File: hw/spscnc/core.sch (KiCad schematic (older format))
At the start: 41 parts, among them J11 Conn_01x04, J7 USB_B_Micro, Q11 BSP41, Q12 BSP42, U3 NCP1117ST33T3G, U4 ESP32-WROOM-32D, U8 FT232RL

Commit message: .
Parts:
- added R? (x4): 47, Resistor_SMD:R_0805_2012Metric, symbol Device:R_Small
- added R? (x2): 1K, Resistor_SMD:R_0603_1608Metric, symbol Device:R_Small
- added U?: 74HC595, symbol 74xx:74HCT595
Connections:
- net labels added: DIR_A, DIR_B, I2S_BITCLK, I2S_DATA, I2S_WORDSTROBE, MTDI, STEP_A, STEP_B, ~I2S_ENABLE
- wire segments 91 -> 101
- no-connect marks 16 -> 17
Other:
- note added: "BOOT MODE:\nMTDI 0 => 3v3 SPI\nGPIO0 1 => Boot APP\nGPIO2 0 => Download\nMTDO 0 => Silent UART / SDIO Sample Fall\nGPIO5 SDIO Launch Fall"
- note added: "TODO:\nchange fluidnc config and attempt to boot.\ncheck bootmode is ok with GPIO signals\ncheck pulses during boot on output pins.\n"
- moved on the sheet: C27, C29, D10, R172, R179, R180, R181, R54, U4

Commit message: halfway changes to support additional axis and to extend over i2so
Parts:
- removed R172, R?: 1K, Resistor_SMD:R_0603_1608Metric, symbol Device:R_Small
- removed R? (x4): 47, Resistor_SMD:R_0805_2012Metric, symbol Device:R_Small
- removed U?: 74HC595, symbol 74xx:74HCT595
- added R187, R188, R189, R190: 47, Resistor_SMD:R_0805_2012Metric, symbol Device:R_Small
- added R191, R64, R65: 1K, Resistor_SMD:R_0603_1608Metric, symbol Device:R_Small
- added U13, U14: 74HC595, symbol 74xx:74HCT595
- gave numbers to parts that had none: 1
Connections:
- net labels added: I2SB
- wire segments 101 -> 113
- no-connect marks 17 -> 23
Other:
- moved on the sheet: C27, C29, C31, C32, C33, D10, R172, R175, R176, R177, R178, R182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

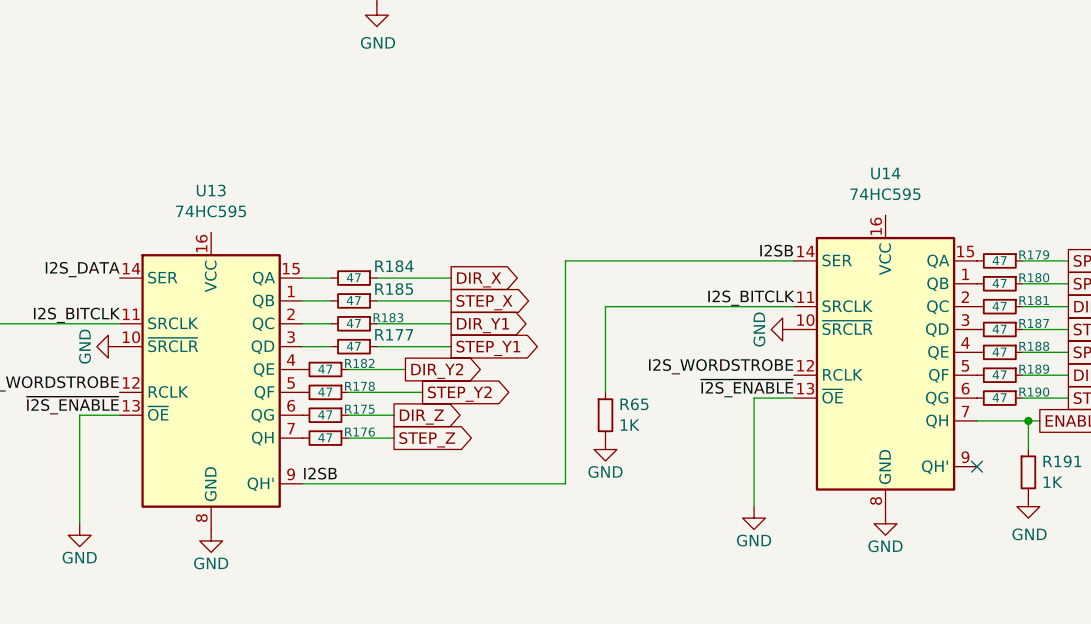
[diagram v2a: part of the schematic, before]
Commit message: added most corrections on the schematic for i2s operation.
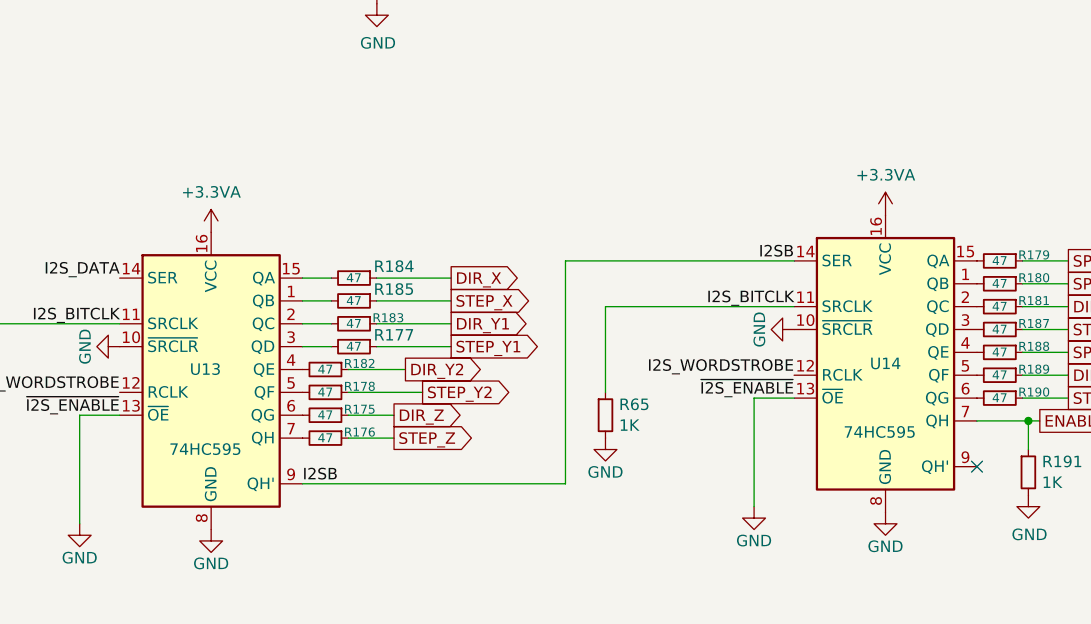
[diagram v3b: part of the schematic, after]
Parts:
- U13, U14: footprint (none) -> Package_SO:SOIC-16_3.9x9.9mm_P1.27mm
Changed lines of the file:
@@
 $Descr A4 11693 8268
 encoding utf-8
-Sheet 6 16
+Sheet 6 17
 Title "Trinamic FluidNC CNC Controller"
 Date "2022-01-27"
@@
 U 1 1 62063E4D
 P 6000 5275
-F 0 "U13" H 6000 6056 50  0000 C CNN
-F 1 "74HC595" H 6000 5965 50  0000 C CNN
-F 2 "" H 6000 5275 50  0001 C CNN
+F 0 "U13" H 5975 5275 50  0000 C CNN
+F 1 "74HC595" H 5975 4925 50  0000 C CNN
+F 2 "Package_SO:SOIC-16_3.9x9.9mm_P1.27mm" H 6000 5275 50  0001 C CNN
 F 3 "https://assets.nexperia.com/documents/data-sheet/74HC_HCT595.pdf" H 6000 5275 50  0001 C CNN
 F 4 "C5947" H 6000 5275 50  0001 C CNN "jlcpcb"
@@
 U 1 1 620F06E6
 P 8950 5200
-F 0 "U14" H 8950 5981 50  0000 C CNN
-F 1 "74HC595" H 8950 5890 50  0000 C CNN
-F 2 "" H 8950 5200 50  0001 C CNN
+F 0 "U14" H 8950 5150 50  0000 C CNN
+F 1 "74HC595" H 8925 4850 50  0000 C CNN
+F 2 "Package_SO:SOIC-16_3.9x9.9mm_P1.27mm" H 8950 5200 50  0001 C CNN
 F 3 "https://assets.nexperia.com/documents/data-sheet/74HC_HCT595.pdf" H 8950 5200 50  0001 C CNN
 F 4 "C5947" H 8950 5200 50  0001 C CNN "jlcpcb"
@@
 NoConn ~ 7375 2775
 NoConn ~ 7325 1475
+$Comp
+L power:+3.3VA-power #PWR?
+U 1 1 623077B6
+P 6000 4675
+AR Path="/61367F02/623077B6" Ref="#PWR?"  Part="1"
+AR Path="/5AD46BE5/619A452E/61B9A8A6/623077B6" Ref="#PWR?"  Part="1"
+AR Path="/61B9A8A6/623077B6" Ref="#PWR?"  Part="1"
+AR Path="/61C743E7/61B9A8A6/623077B6" Ref="#PWR?"  Part="1"
+AR Path="/61C81F9D/623077B6" Ref="#PWR0266"  Part="1"
+AR Path="/623077B6" Ref="#PWR?"  Part="1"
+F 0 "#PWR0266" H 6000 4525 50  0001 C CNN
+F 1 "+3.3VA" H 6000 4850 50  0000 C CNN
+F 2 "" H 6000 4675 50  0001 C CNN
+F 3 "" H 6000 4675 50  0001 C CNN
+	1    6000 4675
+	1    0    0    -1
+$EndComp
+$Comp
+L power:+3.3VA-power #PWR?
+U 1 1 6230AD42
+P 8950 4600
+AR Path="/61367F02/6230AD42" Ref="#PWR?"  Part="1"
+AR Path="/5AD46BE5/619A452E/61B9A8A6/6230AD42" Ref="#PWR?"  Part="1"
+AR Path="/61B9A8A6/6230AD42" Ref="#PWR?"  Part="1"
+AR Path="/61C743E7/61B9A8A6/6230AD42" Ref="#PWR?"  Part="1"
+AR Path="/61C81F9D/6230AD42" Ref="#PWR0267"  Part="1"
+AR Path="/6230AD42" Ref="#PWR?"  Part="1"
+F 0 "#PWR0267" H 8950 4450 50  0001 C CNN
+F 1 "+3.3VA" H 8950 4775 50  0000 C CNN
+F 2 "" H 8950 4600 50  0001 C CNN
+F 3 "" H 8950 4600 50  0001 C CNN
+	1    8950 4600
+	1    0    0    -1
+$EndComp
 $EndSCHEMATC

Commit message: Improved and validated config file
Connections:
- wire segments 113 -> 114
- no-connect marks 23 -> 21
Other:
- moved on the sheet: R180, R188, R191
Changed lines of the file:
@@
 Wire Wire Line
 	7375 2775 7325 2775
-Wire Wire Line
-	7375 2875 7325 2875
 Text GLabel 7325 3275 2    50   Input ~ 0
 LIM_Y1
@@
 Text Notes 12525 3900 0    50   ~ 0
 TODO:\nchange fluidnc config and attempt to boot.\ncheck bootmode is ok with GPIO signals\ncheck pulses during boot on output pins.\n
-Text GLabel 9750 4900 2    50   Output ~ 0
+Text GLabel 7775 1475 2    50   Output ~ 0
 SPINDLE_EN
-Text GLabel 9625 5500 2    50   Output ~ 0
+Text GLabel 8650 2875 2    50   Output ~ 0
 ENABLE_STEPPERS
-Text GLabel 9750 5200 2    50   Output ~ 0
+Text GLabel 7800 2075 2    50   Output ~ 0
 SPINDLE_PWM
 Text GLabel 9750 4800 2    50   Output ~ 0
@@
 L Device:R_Small R?
 U 1 1 62063E2A
-P 9575 5725
+P 8600 3100
 AR Path="/61367F02/62063E2A" Ref="R?"  Part="1"
 AR Path="/5AD46BE5/619A452E/61B9A8A6/62063E2A" Ref="R?"  Part="1"
@@
 AR Path="/61C743E7/61B9A8A6/62063E2A" Ref="R?"  Part="1"
 AR Path="/61C81F9D/62063E2A" Ref="R191"  Part="1"
-F 0 "R191" H 9634 5771 50  0000 L CNN
-F 1 "1K" H 9634 5680 50  0000 L CNN
-F 2 "Resistor_SMD:R_0603_1608Metric" H 9575 5725 50  0001 C CNN
-F 3 "~" H 9575 5725 50  0001 C CNN
-F 4 "C21190" H 9575 5725 50  0001 C CNN "jlcpcb"
-	1    9575 5725
+F 0 "R191" H 8659 3146 50  0000 L CNN
+F 1 "1K" H 8659 3055 50  0000 L CNN
+F 2 "Resistor_SMD:R_0603_1608Metric" H 8600 3100 50  0001 C CNN
+F 3 "~" H 8600 3100 50  0001 C CNN
+F 4 "C21190" H 8600 3100 50  0001 C CNN "jlcpcb"
+	1    8600 3100
 	1    0    0    -1
 $EndComp
@@
 L power:GND-power #PWR?
 U 1 1 62063E31
-P 9575 5825
+P 8600 3200
 AR Path="/61367F02/62063E31" Ref="#PWR?"  Part="1"
 AR Path="/5AD46BE5/619A452E/61B9A8A6/62063E31" Ref="#PWR?"  Part="1"
@@
 AR Path="/61C81F9D/62063E31" Ref="#PWR0129"  Part="1"
 AR Path="/62063E31" Ref="#PWR?"  Part="1"
-F 0 "#PWR0129" H 9575 5575 50  0001 C CNN
-F 1 "GND" H 9580 5652 50  0000 C CNN
-F 2 "" H 9575 5825 50  0001 C CNN
-F 3 "" H 9575 5825 50  0001 C CNN
-	1    9575 5825
+F 0 "#PWR0129" H 8600 2950 50  0001 C CNN
+F 1 "GND" H 8605 3027 50  0000 C CNN
+F 2 "" H 8600 3200 50  0001 C CNN
+F 3 "" H 8600 3200 50  0001 C CNN
+	1    8600 3200
 	1    0    0    -1
 $EndComp
@@
 L Device:R_Small R?
 U 1 1 62063E3F
-P 9450 5200
+P 7500 2075
 AR Path="/62063E3F" Ref="R?"  Part="1"
 AR Path="/61C81F9D/62063E3F" Ref="R188"  Part="1"
-F 0 "R188" V 9425 5350 39  0000 C CNN
-F 1 "47" V 9450 5200 39  0000 C CNN
-F 2 "Resistor_SMD:R_0805_2012Metric" V 9380 5200 50  0001 C CNN
-F 3 "~" H 9450 5200 50  0001 C CNN
-F 4 "C17714" H 9450 5200 50  0001 C CNN "jlcpcb"
-	1    9450 5200
+F 0 "R188" V 7475 2225 39  0000 C CNN
+F 1 "47" V 7500 2075 39  0000 C CNN
+F 2 "Resistor_SMD:R_0805_2012Metric" V 7430 2075 50  0001 C CNN
+F 3 "~" H 7500 2075 50  0001 C CNN
+F 4 "C17714" H 7500 2075 50  0001 C CNN "jlcpcb"
+	1    7500 2075
 	0    1    1    0
 $EndComp
@@
 L Device:R_Small R?
 U 1 1 62063E46
-P 9450 4900
+P 7475 1475
 AR Path="/62063E46" Ref="R?"  Part="1"
 AR Path="/61C81F9D/62063E46" Ref="R180"  Part="1"
-F 0 "R180" V 9425 5050 39  0000 C CNN
-F 1 "47" V 9450 4900 39  0000 C CNN
-F 2 "Resistor_SMD:R_0805_2012Metric" V 9380 4900 50  0001 C CNN
-F 3 "~" H 9450 4900 50  0001 C CNN
-F 4 "C17714" H 9450 4900 50  0001 C CNN "jlcpcb"
-	1    9450 4900
+F 0 "R180" V 7450 1625 39  0000 C CNN
+F 1 "47" V 7475 1475 39  0000 C CNN
+F 2 "Resistor_SMD:R_0805_2012Metric" V 7405 1475 50  0001 C CNN
+F 3 "~" H 7475 1475 50  0001 C CNN
+F 4 "C17714" H 7475 1475 50  0001 C CNN "jlcpcb"
+	1    7475 1475
 	0    1    1    0
 $EndComp
@@
 	9750 4800 9550 4800
 Wire Wire Line
-	9550 5200 9750 5200
-Wire Wire Line
-	9550 4900 9750 4900
+	7600 2075 7800 2075
+Wire Wire Line
+	7575 1475 7775 1475
 Text GLabel 9750 5000 2    50   Output ~ 0
 DIR_A
@@
 	8375 5400 8375 5875
 Wire Wire Line
-	9575 5625 9575 5500
-Connection ~ 9575 5500
-Wire Wire Line
-	9575 5500 9625 5500
-Wire Wire Line
-	9350 5500 9575 5500
+	8600 3000 8600 2875
+Connection ~ 8600 2875
+Wire Wire Line
+	8600 2875 8650 2875
 Text Label 6400 5775 0    50   ~ 0
 I2SB
@@
 NoConn ~ 7325 1775
 NoConn ~ 7325 1875
-NoConn ~ 7325 2075
-NoConn ~ 7375 2875
 NoConn ~ 7375 2775
-NoConn ~ 7325 1475
 $Comp
 L power:+3.3VA-power #PWR?
@@
 	1    0    0    -1
 $EndComp
+Wire Wire Line
+	7325 2875 8600 2875
+NoConn ~ 9350 5500
+Wire Wire Line
+	7375 1475 7325 1475
+Wire Wire Line
+	7400 2075 7325 2075
 $EndSCHEMATC

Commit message: began routing of the i2so part
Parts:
- removed R65: 1K, Resistor_SMD:R_0603_1608Metric, symbol Device:R_Small
- added C91, C92: 100nF, Capacitor_SMD:C_0603_1608Metric, symbol Device:C
- added D55: LED, Diode_SMD:D_0805_2012Metric, symbol Device:LED
- added R194: 10K, Resistor_SMD:R_0805_2012Metric, symbol Device:R
- added R195, R196: 47, Resistor_SMD:R_0805_2012Metric, symbol Device:R_Small
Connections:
- net labels added: ENABLE_VACUUM
- wire segments 114 -> 118
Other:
- note added: "CHECKS:\n[OK] change fluidnc config and attempt to boot.\n[OK] check bootmode is ok with GPIO signals\ncheck pulses during boot on output pins.\n"
- note removed: "TODO:\nchange fluidnc config and attempt to boot.\ncheck bootmode is ok with GPIO signals\ncheck pulses during boot on output pins.\n"
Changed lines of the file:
@@
 Text GLabel 6125 1375 0    50   Input ~ 0
 Hold
-Text GLabel 8625 1675 2    50   Input ~ 0
+Text GLabel 8800 1675 2    50   Input ~ 0
 Reset
 Text GLabel 7475 3175 2    50   Input ~ 0
 Door
 Wire Wire Line
-	8625 1675 8500 1675
+	8800 1675 8500 1675
 Wire Wire Line
 	7325 1975 7425 1975
@@
 Wire Wire Line
 	6800 5575 6600 5575
-Text Label 7450 2575 0    50   ~ 0
+Text Label 8125 2575 0    50   ~ 0
 I2S_BITCLK
-Text Label 7450 2475 0    50   ~ 0
+Text Label 8125 2475 0    50   ~ 0
 I2S_DATA
 Text Label 7450 2175 0    50   ~ 0
@@
 BOOT MODE:\nMTDI 0 => 3v3 SPI\nGPIO0 1 => Boot APP\nGPIO2 0 => Download\nMTDO 0 => Silent UART / SDIO Sample Fall\nGPIO5 SDIO Launch Fall
 Text Notes 12525 3900 0    50   ~ 0
-TODO:\nchange fluidnc config and attempt to boot.\ncheck bootmode is ok with GPIO signals\ncheck pulses during boot on output pins.\n
+CHECKS:\n[OK] change fluidnc config and attempt to boot.\n[OK] check bootmode is ok with GPIO signals\ncheck pulses during boot on output pins.\n
 Text GLabel 7775 1475 2    50   Output ~ 0
 SPINDLE_EN
@@
 Text Label 8550 5400 2    50   ~ 0
 ~I2S_ENABLE
-Wire Wire Line
-	8550 5000 7725 5000
-Wire Wire Line
-	7725 5000 7725 5375
-$Comp
-L Device:R_Small R?
-U 1 1 620F09CF
-P 7725 5475
-AR Path="/61367F02/620F09CF" Ref="R?"  Part="1"
-AR Path="/5AD46BE5/619A452E/61B9A8A6/620F09CF" Ref="R?"  Part="1"
-AR Path="/61B9A8A6/620F09CF" Ref="R?"  Part="1"
-AR Path="/61C743E7/61B9A8A6/620F09CF" Ref="R?"  Part="1"
-AR Path="/61C81F9D/620F09CF" Ref="R65"  Part="1"
-F 0 "R65" H 7784 5521 50  0000 L CNN
-F 1 "1K" H 7784 5430 50  0000 L CNN
-F 2 "Resistor_SMD:R_0603_1608Metric" H 7725 5475 50  0001 C CNN
-F 3 "~" H 7725 5475 50  0001 C CNN
-F 4 "C21190" H 7725 5475 50  0001 C CNN "jlcpcb"
-	1    7725 5475
-	1    0    0    -1
-$EndComp
-$Comp
-L power:GND-power #PWR?
-U 1 1 620F09D9
-P 7725 5575
-AR Path="/5AD46BE5/620F09D9" Ref="#PWR?"  Part="1"
-AR Path="/5AD46BE5/619A452E/620F09D9" Ref="#PWR?"  Part="1"
-AR Path="/620F09D9" Ref="#PWR?"  Part="1"
-AR Path="/61B9A8A6/620F09D9" Ref="#PWR?"  Part="1"
-AR Path="/61C743E7/61B9A8A6/620F09D9" Ref="#PWR?"  Part="1"
-AR Path="/61C81F9D/620F09D9" Ref="#PWR063"  Part="1"
-F 0 "#PWR063" H 7725 5325 50  0001 C CNN
-F 1 "GND" H 7725 5425 50  0000 C CNN
-F 2 "" H 7725 5575 50  0001 C CNN
-F 3 "" H 7725 5575 50  0001 C CNN
-	1    7725 5575
-	-1   0    0    -1
-$EndComp
 $Comp
 L power:GND-power #PWR?
@@
 Wire Wire Line
 	7325 2875 8600 2875
-NoConn ~ 9350 5500
 Wire Wire Line
 	7375 1475 7325 1475
 Wire Wire Line
 	7400 2075 7325 2075
+NoConn ~ 9350 5200
+$Comp
+L Device:R R?
+U 1 1 620708E2
+P 9675 6100
+AR Path="/5AD47FD6/620708E2" Ref="R?"  Part="1"
+AR Path="/61FBB705/620708E2" Ref="R?"  Part="1"
+AR Path="/5AD46BE5/620708E2" Ref="R?"  Part="1"
+AR Path="/5AD46BE5/619A452E/620708E2" Ref="R?"  Part="1"
+AR Path="/620708E2" Ref="R?"  Part="1"
+AR Path="/61B9A8A6/620708E2" Ref="R?"  Part="1"
+AR Path="/61C743E7/61B9A8A6/620708E2" Ref="R?"  Part="1"
+AR Path="/61C81F9D/620708E2" Ref="R194"  Part="1"
+F 0 "R194" V 9755 6100 50  0000 C CNN
+F 1 "10K" V 9675 6100 50  0000 C CNN
+F 2 "Resistor_SMD:R_0805_2012Metric" V 9605 6100 50  0001 C CNN
+F 3 "" H 9675 6100 50  0001 C CNN
+F 4 "" V 9675 6100 60  0001 C CNN "farnell"
+F 5 "C17414" H 9675 6100 50  0001 C CNN "jlcpcb"
+F 6 "5%" H 9675 6100 50  0001 C CNN "precision"
+F 7 "1%" H 9675 6100 50  0001 C CNN "power"
+	1    9675 6100
+	1    0    0    -1
+$EndComp
+$Comp
+L Device:LED D?
+U 1 1 620708EF
+P 9675 5750
+AR Path="/5AD47FD6/620708EF" Ref="D?"  Part="1"
+AR Path="/61FBB705/620708EF" Ref="D?"  Part="1"
+AR Path="/5AD46BE5/620708EF" Ref="D?"  Part="1"
+AR Path="/5AD46BE5/619A452E/620708EF" Ref="D?"  Part="1"
+AR Path="/620708EF" Ref="D?"  Part="1"
+AR Path="/61B9A8A6/620708EF" Ref="D?"  Part="1"
+AR Path="/61C743E7/61B9A8A6/620708EF" Ref="D?"  Part="1"
+AR Path="/61C81F9D/620708EF" Ref="D55"  Part="1"
+F 0 "D55" H 9675 5850 50  0000 C CNN
+F 1 "LED" H 9675 5650 50  0000 C CNN
+F 2 "Diode_SMD:D_0805_2012Metric" H 9675 5750 50  0001 C CNN
+F 3 "" H 9675 5750 50  0001 C CNN
+F 4 "" H 9675 5750 60  0001 C CNN "farnell"
+F 5 "C84256" H 9675 5750 50  0001 C CNN "jlcpcb"
+F 6 "red" H 9675 5750 50  0001 C CNN "power"
+	1    9675 5750
+	0    -1   -1   0
+$EndComp
+Wire Wire Line
+	9675 5950 9675 5900
+Wire Wire Line
+	9350 5500 9675 5500
+Wire Wire Line
+	9675 5500 9675 5600
+$Comp
+L power:GND-power #PWR?
+U 1 1 62082702
+P 9675 6250
+AR Path="/5AD46BE5/62082702" Ref="#PWR?"  Part="1"
+AR Path="/5AD46BE5/619A452E/62082702" Ref="#PWR?"  Part="1"
+AR Path="/62082702" Ref="#PWR?"  Part="1"
+AR Path="/61B9A8A6/62082702" Ref="#PWR?"  Part="1"
+AR Path="/61C743E7/61B9A8A6/62082702" Ref="#PWR?"  Part="1"
+AR Path="/61C81F9D/62082702" Ref="#PWR0268"  Part="1"
+F 0 "#PWR0268" H 9675 6000 50  0001 C CNN
+F 1 "GND" H 9675 6100 50  0000 C CNN
+F 2 "" H 9675 6250 50  0001 C CNN
+F 3 "" H 9675 6250 50  0001 C CNN
+	1    9675 6250
+	-1   0    0    -1
+$EndComp
+$Comp
+L Device:R_Small R?
+U 1 1 62091D8C
+P 7550 2475
+AR Path="/62091D8C" Ref="R?"  Part="1"
+AR Path="/61C81F9D/62091D8C" Ref="R195"  Part="1"
+F 0 "R195" V 7500 2650 50  0000 C CNN
+F 1 "47" V 7550 2475 39  0000 C CNN
+F 2 "Resistor_SMD:R_0805_2012Metric" V 7480 2475 50  0001 C CNN
+F 3 "~" H 7550 2475 50  0001 C CNN
+F 4 "C17714" H 7550 2475 50  0001 C CNN "jlcpcb"
+	1    7550 2475
+	0    1    1    0
+$EndComp
+$Comp
+L Device:R_Small R?
+U 1 1 620A09FA
+P 7550 2575
+AR Path="/620A09FA" Ref="R?"  Part="1"
+AR Path="/61C81F9D/620A09FA" Ref="R196"  Part="1"
+F 0 "R196" V 7500 2750 50  0000 C CNN
+F 1 "47" V 7550 2575 39  0000 C CNN
+F 2 "Resistor_SMD:R_0805_2012Metric" V 7480 2575 50  0001 C CNN
+F 3 "~" H 7550 2575 50  0001 C CNN
+F 4 "C17714" H 7550 2575 50  0001 C CNN "jlcpcb"
+	1    7550 2575
+	0    1    1    0
+$EndComp
+Wire Wire Line
+	7650 2575 8125 2575
+Wire Wire Line
+	8125 2475 7650 2475
+Text GLabel 9750 4900 2    50   Output ~ 0
+ENABLE_VACUUM
+Wire Wire Line
+	9750 4900 9350 4900
+$Comp
+L Device:C C?
+U 1 1 621362CC
+P 5825 6975
+AR Path="/61E601B6/621362CC" Ref="C?"  Part="1"
+AR Path="/6203D74D/621362CC" Ref="C?"  Part="1"
+AR Path="/6203DA5D/621362CC" Ref="C?"  Part="1"
+AR Path="/6203DFCF/621362CC" Ref="C?"  Part="1"
+AR Path="/6221509B/621362CC" Ref="C?"  Part="1"
+AR Path="/61C81F9D/621362CC" Ref="C91"  Part="1"
+F 0 "C91" V 6100 7000 50  0000 C CNN
+F 1 "100nF" V 5975 6950 50  0000 C CNN
+F 2 "Capacitor_SMD:C_0603_1608Metric" H 5863 6825 50  0001 C CNN
+F 3 "~" H 5825 6975 50  0001 C CNN
+F 4 "C14663" H 5825 6975 50  0001 C CNN "jlcpcb"
+	1    5825 6975
+	-1   0    0    1
+$EndComp
+$Comp
+L Device:C C?
+U 1 1 6213BF1D
+P 6275 6975
+AR Path="/61E601B6/6213BF1D" Ref="C?"  Part="1"
+AR Path="/6203D74D/6213BF1D" Ref="C?"  Part="1"
+AR Path="/6203DA5D/6213BF1D" Ref="C?"  Part="1"
+AR Path="/6203DFCF/6213BF1D" Ref="C?"  Part="1"
+AR Path="/6221509B/6213BF1D" Ref="C?"  Part="1"
+AR Path="/61C81F9D/6213BF1D" Ref="C92"  Part="1"
+F 0 "C92" V 6550 7000 50  0000 C CNN
+F 1 "100nF" V 6425 6950 50  0000 C CNN
+F 2 "Capacitor_SMD:C_0603_1608Metric" H 6313 6825 50  0001 C CNN
+F 3 "~" H 6275 6975 50  0001 C CNN
+F 4 "C14663" H 6275 6975 50  0001 C CNN "jlcpcb"
+	1    6275 6975
+	-1   0    0    1
+$EndComp
+$Comp
+L power:GND-power #PWR?
+U 1 1 621409CC
+P 6275 7125
+AR Path="/5AD46BE5/621409CC" Ref="#PWR?"  Part="1"
+AR Path="/5AD46BE5/619A452E/621409CC" Ref="#PWR?"  Part="1"
+AR Path="/621409CC" Ref="#PWR?"  Part="1"
+AR Path="/61B9A8A6/621409CC" Ref="#PWR?"  Part="1"
+AR Path="/61C743E7/61B9A8A6/621409CC" Ref="#PWR?"  Part="1"
+AR Path="/61C81F9D/621409CC" Ref="#PWR0168"  Part="1"
+F 0 "#PWR0168" H 6275 6875 50  0001 C CNN
+F 1 "GND" H 6275 6975 50  0000 C CNN
+F 2 "" H 6275 7125 50  0001 C CNN
+F 3 "" H 6275 7125 50  0001 C CNN
+	1    6275 7125
+	-1   0    0    -1
+$EndComp
+$Comp
+L power:GND-power #PWR?
+U 1 1 62140D17
+P 5825 7125
+AR Path="/5AD46BE5/62140D17" Ref="#PWR?"  Part="1"
+AR Path="/5AD46BE5/619A452E/62140D17" Ref="#PWR?"  Part="1"
+AR Path="/62140D17" Ref="#PWR?"  Part="1"
+AR Path="/61B9A8A6/62140D17" Ref="#PWR?"  Part="1"
+AR Path="/61C743E7/61B9A8A6/62140D17" Ref="#PWR?"  Part="1"
+AR Path="/61C81F9D/62140D17" Ref="#PWR0164"  Part="1"
+F 0 "#PWR0164" H 5825 6875 50  0001 C CNN
+F 1 "GND" H 5825 6975 50  0000 C CNN
+F 2 "" H 5825 7125 50  0001 C CNN
+F 3 "" H 5825 7125 50  0001 C CNN
+	1    5825 7125
+	-1   0    0    -1
+$EndComp
+$Comp
+L power:+3.3VA-power #PWR?
+U 1 1 621421A9
+P 5825 6825
+AR Path="/61367F02/621421A9" Ref="#PWR?"  Part="1"
+AR Path="/5AD46BE5/619A452E/61B9A8A6/621421A9" Ref="#PWR?"  Part="1"
+AR Path="/61B9A8A6/621421A9" Ref="#PWR?"  Part="1"
+AR Path="/61C743E7/61B9A8A6/621421A9" Ref="#PWR?"  Part="1"
+AR Path="/61C81F9D/621421A9" Ref="#PWR063"  Part="1"
+AR Path="/621421A9" Ref="#PWR?"  Part="1"
+F 0 "#PWR063" H 5825 6675 50  0001 C CNN
+F 1 "+3.3VA" H 5825 7000 50  0000 C CNN
+F 2 "" H 5825 6825 50  0001 C CNN
+F 3 "" H 5825 6825 50  0001 C CNN
+	1    5825 6825
+	1    0    0    -1
+$EndComp
+$Comp
+L power:+3.3VA-power #PWR?
+U 1 1 62142C2C
+P 6275 6825
+AR Path="/61367F02/62142C2C" Ref="#PWR?"  Part="1"
+AR Path="/5AD46BE5/619A452E/61B9A8A6/62142C2C" Ref="#PWR?"  Part="1"
+AR Path="/61B9A8A6/62142C2C" Ref="#PWR?"  Part="1"
+AR Path="/61C743E7/61B9A8A6/62142C2C" Ref="#PWR?"  Part="1"
+AR Path="/61C81F9D/62142C2C" Ref="#PWR0165"  Part="1"
+AR Path="/62142C2C" Ref="#PWR?"  Part="1"
+F 0 "#PWR0165" H 6275 6675 50  0001 C CNN
+F 1 "+3.3VA" H 6275 7000 50  0000 C CNN
+F 2 "" H 6275 6825 50  0001 C CNN
+F 3 "" H 6275 6825 50  0001 C CNN
+	1    6275 6825
+	1    0    0    -1
+$EndComp
 $EndSCHEMATC
